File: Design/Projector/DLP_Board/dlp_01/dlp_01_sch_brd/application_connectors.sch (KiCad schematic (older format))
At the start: 1 part

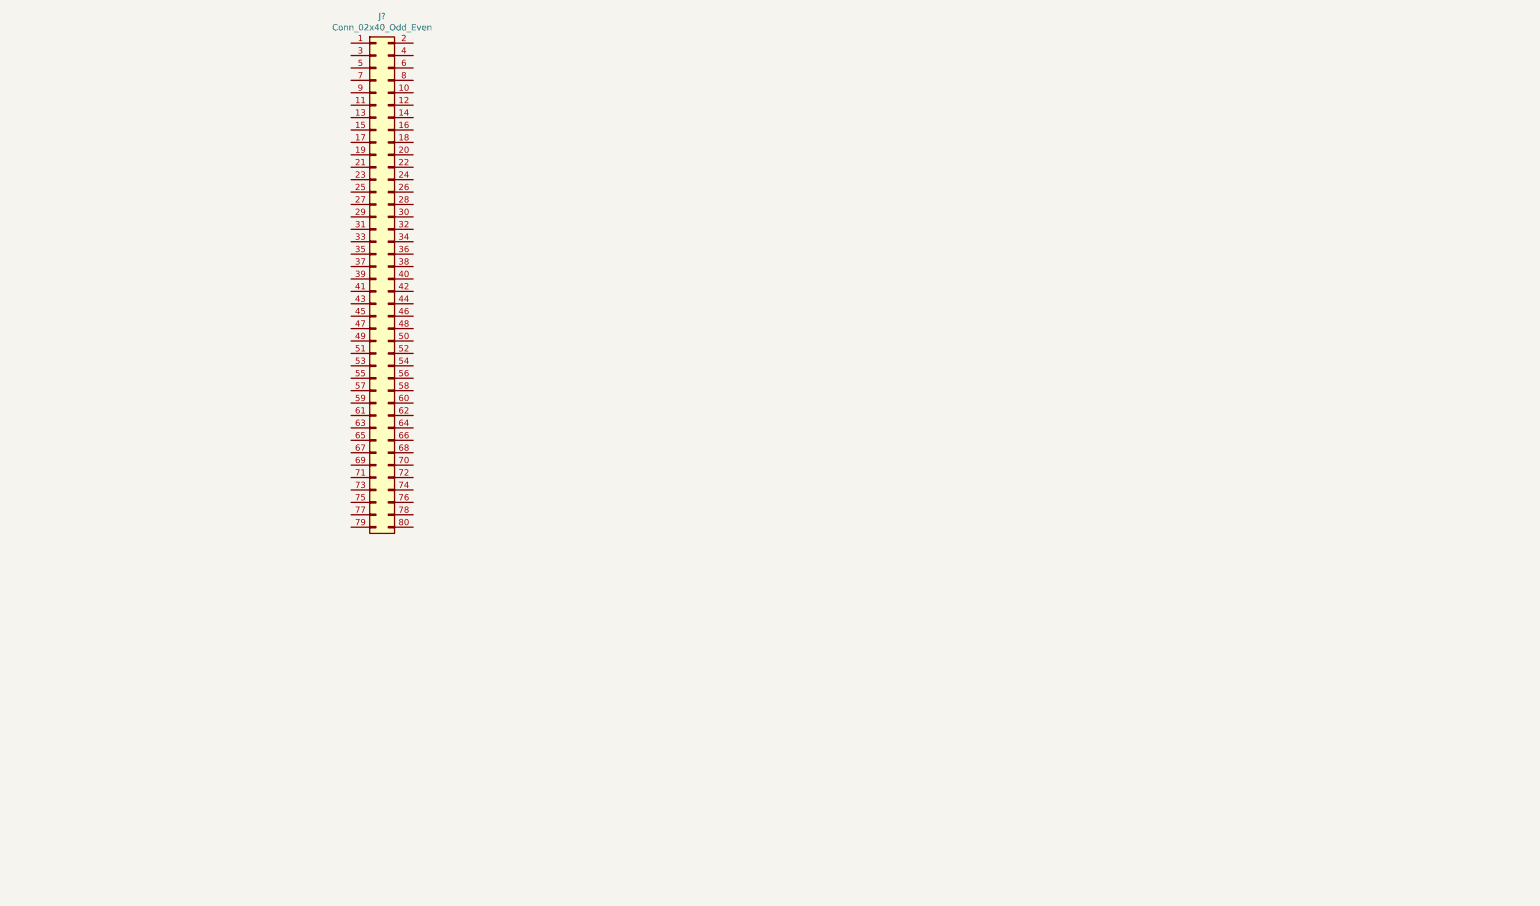
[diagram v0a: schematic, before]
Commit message: Updated schematic with changes pulling together top level design
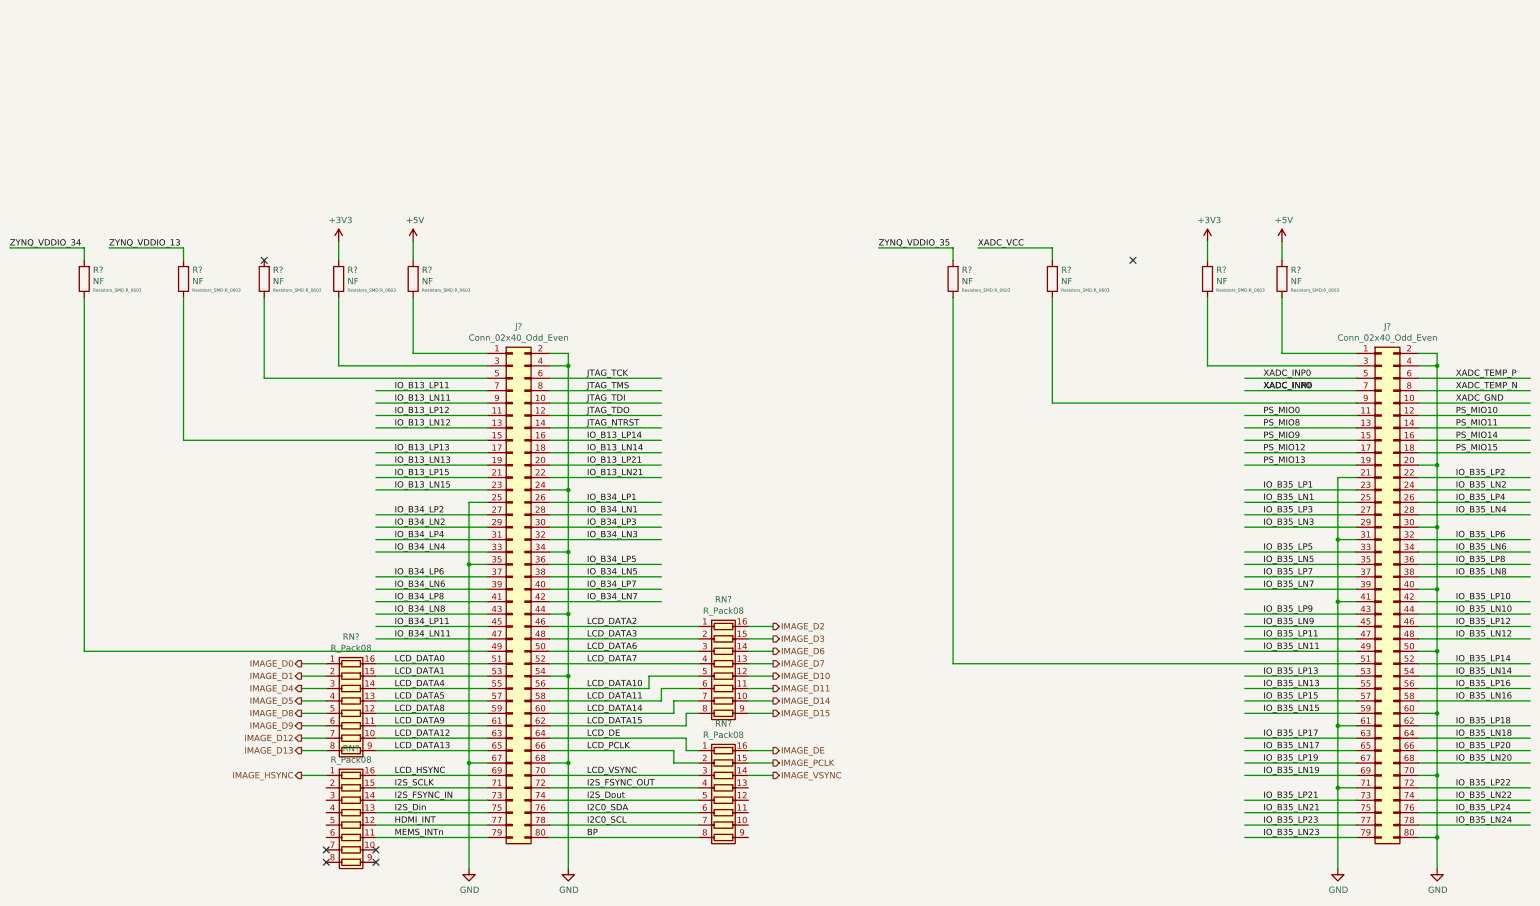
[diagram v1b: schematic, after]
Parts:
- added J?: Conn_02x40_Odd_Even, symbol Connector_Generic:Conn_02x40_Odd_Even
- added R? (x9): NF, Resistors_SMD:R_0603, symbol Device:R
- added RN? (x4): R_Pack08, symbol Device:R_Pack08
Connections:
- net labels added: +3V3, +5V, BP, GND, HDMI_INT, I2C0_SCL, I2C0_SDA, I2S_Din, I2S_Dout, I2S_FSYNC_IN, I2S_FSYNC_OUT, I2S_SCLK, IMAGE_D0, IMAGE_D1, IMAGE_D10, IMAGE_D11, IMAGE_D12, IMAGE_D13, IMAGE_D14, IMAGE_D15, IMAGE_D2, IMAGE_D3, IMAGE_D4, IMAGE_D5, IMAGE_D6, IMAGE_D7, IMAGE_D8, IMAGE_D9, IMAGE_DE, IMAGE_HSYNC, IMAGE_PCLK, IMAGE_VSYNC, IO_B13_LN11, IO_B13_LN12, IO_B13_LN13, IO_B13_LN14, IO_B13_LN15, IO_B13_LN21, IO_B13_LP11, IO_B13_LP12, IO_B13_LP13, IO_B13_LP14, IO_B13_LP15, IO_B13_LP21, IO_B34_LN1, IO_B34_LN11, IO_B34_LN2, IO_B34_LN3, IO_B34_LN4, IO_B34_LN5, IO_B34_LN6, IO_B34_LN7, IO_B34_LN8, IO_B34_LP1, IO_B34_LP11, IO_B34_LP2, IO_B34_LP3, IO_B34_LP4, IO_B34_LP5, IO_B34_LP6, IO_B34_LP7, IO_B34_LP8, IO_B35_LN1, IO_B35_LN10, IO_B35_LN11, IO_B35_LN12, IO_B35_LN13, IO_B35_LN14, IO_B35_LN15, IO_B35_LN16, IO_B35_LN17, IO_B35_LN18, IO_B35_LN19, IO_B35_LN2, IO_B35_LN20, IO_B35_LN21, IO_B35_LN22, IO_B35_LN23, IO_B35_LN24, IO_B35_LN3, IO_B35_LN4, IO_B35_LN5, IO_B35_LN6, IO_B35_LN7, IO_B35_LN8, IO_B35_LN9, IO_B35_LP1, IO_B35_LP10, IO_B35_LP11, IO_B35_LP12, IO_B35_LP13, IO_B35_LP14, IO_B35_LP15, IO_B35_LP16, IO_B35_LP17, IO_B35_LP18, IO_B35_LP19, IO_B35_LP2, IO_B35_LP20, IO_B35_LP21, IO_B35_LP22, IO_B35_LP23, IO_B35_LP24, IO_B35_LP3, IO_B35_LP4, IO_B35_LP5, IO_B35_LP6, IO_B35_LP7, IO_B35_LP8, IO_B35_LP9, JTAG_NTRST, JTAG_TCK, JTAG_TDI, JTAG_TDO, JTAG_TMS, LCD_DATA0, LCD_DATA1, LCD_DATA10, LCD_DATA11, LCD_DATA12, LCD_DATA13, LCD_DATA14, LCD_DATA15, LCD_DATA2, LCD_DATA3, LCD_DATA4, LCD_DATA5, LCD_DATA6, LCD_DATA7, LCD_DATA8, LCD_DATA9, LCD_DE, LCD_HSYNC, LCD_PCLK, LCD_VSYNC, MEMS_INTn, PS_MIO0, PS_MIO10, PS_MIO11, PS_MIO12, PS_MIO13, PS_MIO14, PS_MIO15, PS_MIO8, PS_MIO9, XADC_GND, XADC_INN0, XADC_INP0, XADC_TEMP_N, XADC_TEMP_P, XADC_VCC, ZYNQ_VDDIO_13, ZYNQ_VDDIO_34, ZYNQ_VDDIO_35
- wire segments 0 -> 237
- no-connect marks 0 -> 6
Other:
- moved on the sheet: J?

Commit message: Ongoing updates the schematics
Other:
- moved on the sheet: J?, R?, RN?

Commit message: More updates in the DLP board
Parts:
- removed RN? (x2): R_Pack08, symbol Device:R_Pack08
- added R? (x11): 22R, Resistors_SMD:R_0603, symbol Device:R
- added R? (x3): NF, Resistors_SMD:R_0603, symbol Device:R
- added RN? (x3): 22R, Resistors_SMD:R_Array_Convex_8x0602, symbol Device:R_Pack08
- added RN?: R_Pack08, symbol Device:R_Pack08
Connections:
- net labels added: 3DR_A, 3DR_B, CONTR0_SCL, CONTR0_SDA, CONTR1_SCL, CONTR1_SDA, DATEN_A, DATEN_B, HOST_SCL, HOST_SDA, HSYNC_A, HSYNC_B, PCLK_A, PCLK_B, PDAT_A_10, PDAT_A_11, PDAT_A_12, PDAT_A_13, PDAT_A_14, PDAT_A_15, PDAT_A_16, PDAT_A_17, PDAT_A_18, PDAT_A_19, PDAT_A_2, PDAT_A_20, PDAT_A_21, PDAT_A_22, PDAT_A_23, PDAT_A_3, PDAT_A_4, PDAT_A_5, PDAT_A_6, PDAT_A_7, PDAT_A_8, PDAT_A_9, PDAT_A_[23..0], PDAT_B_0, PDAT_B_1, PDAT_B_10, PDAT_B_11, PDAT_B_12, PDAT_B_13, PDAT_B_14, PDAT_B_15, PDAT_B_16, PDAT_B_17, PDAT_B_18, PDAT_B_19, PDAT_B_2, PDAT_B_20, PDAT_B_21, PDAT_B_22, PDAT_B_23, PDAT_B_3, PDAT_B_4, PDAT_B_5, PDAT_B_6, PDAT_B_7, PDAT_B_8, PDAT_B_9, PDAT_B_[23..0], PDM_CVS_TE_A, PDM_CVS_TE_B, PL_SCL, PL_SDA, PS_SCL, PS_SDA, VSYNC_A, VSYNC_B
- net labels removed: IMAGE_D0, IMAGE_D1, IMAGE_D10, IMAGE_D11, IMAGE_D12, IMAGE_D13, IMAGE_D14, IMAGE_D15, IMAGE_D2, IMAGE_D3, IMAGE_D4, IMAGE_D5, IMAGE_D6, IMAGE_D7, IMAGE_D8, IMAGE_D9, IMAGE_DE, IMAGE_HSYNC, IMAGE_PCLK, IMAGE_VSYNC
- wire segments 237 -> 344
- no-connect marks 6 -> 3
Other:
- note added: "Interfaces to MYiR Z-Turn Board"
- moved on the sheet: J?, R?, RN?

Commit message: Initial placement of power converters, BGA fanout and Z-turn board outline imported
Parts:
- added R100, R101, R102, R103, R104, R105: 22R, Resistors_SMD:R_0603, symbol Device:R
- J1, J2: renamed from J?; footprint (none) -> Pin_Headers:Pin_Header_Straight_2x40_Pitch1.27mm_SMD
- RN1, RN2, RN3: renamed from RN?; footprint (none) -> Resistors_SMD:R_Array_Convex_8x0602
- gave numbers to parts that had none: 26
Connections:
- net labels added: ACT_SYNC, FPGA_RDY, PROJ_ON, SUB_FRAME, mHOST_IRQ, sHOST_IRQ
- wire segments 344 -> 349
- no-connect marks 3 -> 2

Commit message: Schematic and PCB complete ready for review
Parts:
- removed R100, R101, R102, R103, R104, R105, R75, R76, R84, R85, R86, R87, R88, R90: 22R, Resistors_SMD:R_0603, symbol Device:R
- removed R79, R83: NF, Resistors_SMD:R_0603, symbol Device:R
- removed RN1, RN2, RN3: R_Pack08, Resistors_SMD:R_Array_Convex_8x0602, symbol Device:R_Pack08
- removed RN4, RN5, RN6: 22R, Resistors_SMD:R_Array_Convex_8x0602, symbol Device:R_Pack08
- R72, R73, R74: value 22R -> NF
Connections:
- net labels added: +1V8, PDAT_A_0, PDAT_A_1
- net labels removed: 3DR_A, 3DR_B, XADC_VCC
- wire segments 349 -> 252
- no-connect marks 2 -> 3
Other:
- moved on the sheet: R68
